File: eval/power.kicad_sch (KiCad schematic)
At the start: 48 parts, among them Q1 BSC0702LS, Q2 BSC0702LS, Q5 BSC0702LS, Q6 BSC0702LS, U2 LM5148RGYR, U3 INA180A3, U8 INA180A3

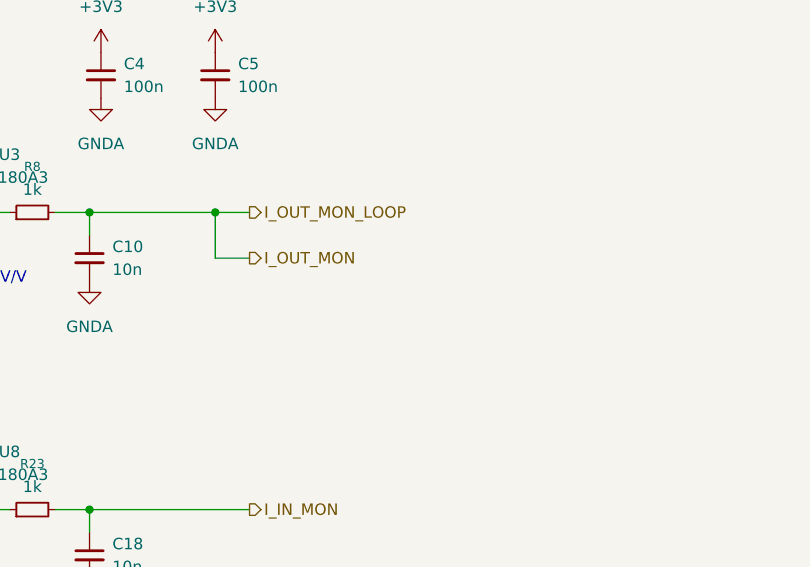
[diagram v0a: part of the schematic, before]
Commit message: [sch]power_battery: add feature voltage drop, current rush, MCU input, reverse protection
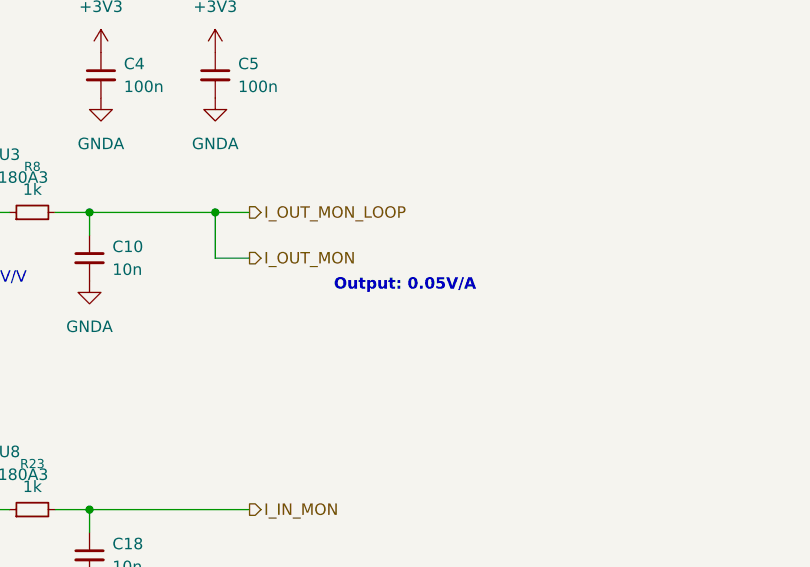
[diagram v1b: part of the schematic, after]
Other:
- note added: "Output: 0.05V/A"
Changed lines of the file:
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@@
+		)
+	)
+	(text "Output: 0.05V/A"
+		(exclude_from_sim no)
+		(at 174.752 222.758 0)
+		(effects
+			(font
+				(size 1.27 1.27)
+				(thickness 0.254)
+				(bold yes)
+			)
 		)
 	)

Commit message: [layout] first draft layout
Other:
- note added: "inductor selection list C18337518 C52989662 C52989661（470n)"
- note removed: "back to back output protect"
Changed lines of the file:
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@@
 	(generator_version "10.0")
 	(paper "A3")
+	(text "inductor selection list\nC18337518\n\nC52989662 \nC52989661（470n)"
+		(exclude_from_sim no)
+		(at 242.57 124.46 0)
+		(effects
+			(font
+				(size 1.27 1.27)
+			)
+		)
+	)
 	(text "RT(frequency config):\nR(kohm) = (10e6/500(kHz)- 53)/45\n[Equation 4 snvsc01]"
 		(exclude_from_sim no)
@@
 		(effects
 			(font
-				(size 1.27 1.27)
-			)
-		)
-	)
-	(text "back to back output protect"
-		(exclude_from_sim no)
-		(at 282.194 149.86 0)
-		(effects
-			(font

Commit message: [layout] 50*100mm, without trace
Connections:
- net GNDPWR: now also Q2.1 (S), Q2.2 (S), Q2.3 (S), Q5.1 (S), Q5.2 (S), Q5.3 (S); no longer Q2.5 (D), Q2.6 (D), Q2.7 (D), Q2.8 (D), Q5.5 (D), Q5.6 (D), Q5.7 (D), Q5.8 (D)
- net IN_ISNS-: now also Q1.5 (D), Q1.6 (D), Q1.7 (D), Q1.8 (D), Q6.5 (D), Q6.6 (D), Q6.7 (D), Q6.8 (D); no longer Q1.1 (S), Q1.2 (S), Q1.3 (S), Q6.1 (S), Q6.2 (S), Q6.3 (S)
- net SW: now also Q1.1 (S), Q1.2 (S), Q1.3 (S), Q2.5 (D), Q2.6 (D), Q2.7 (D), Q2.8 (D), Q5.5 (D), Q5.6 (D), Q5.7 (D), Q5.8 (D), Q6.1 (S), Q6.2 (S), Q6.3 (S); no longer C1.2, Q1.5 (D), Q1.6 (D), Q1.7 (D), Q1.8 (D), Q2.1 (S), Q2.2 (S), Q2.3 (S), Q5.1 (S), Q5.2 (S), Q5.3 (S), Q6.5 (D), Q6.6 (D), Q6.7 (D), Q6.8 (D), U2.14 (SW)
- new net: C1.2, U2.14 (SW)
